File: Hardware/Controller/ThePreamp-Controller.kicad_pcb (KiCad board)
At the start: 2 copper layers, 60 x 95.8 mm, 34 parts, among them J1 B1 Relays, J10 I2C (FUTURE USE), J11 ROTARY ENC & SWITCH 1, J12 ROTARY ENC & SWITCH 2, J13 IR RECV, J14 12V, J15 8V, J2 PWR AMP L 12V TRIGGER, J3 PWR AMP L SWITCH, J4 PWR AMP R 12V TRIGGER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

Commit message: Controller pcb dimensions added
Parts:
- removed C1: 0.1uF, Capacitor_SMD:C_0805_2012Metric_Pad1.15x1.40mm_HandSolder
- removed D1, D2: CD4148W, Diode_SMD:D_0805_2012Metric
- removed J1: B1 Relays, Connector_JST:JST_XH_B7B-XH-A_1x07_P2.50mm_Vertical
- removed J10: I2C (FUTURE USE), Connector_JST:JST_XH_B4B-XH-A_1x04_P2.50mm_Vertical
- removed J11: ROTARY ENC & SWITCH 1, Connector_JST:JST_XH_B5B-XH-A_1x05_P2.50mm_Vertical
- removed J12: ROTARY ENC & SWITCH 2, Connector_JST:JST_XH_B5B-XH-A_1x05_P2.50mm_Vertical
- removed J13: IR RECV, Connector_JST:JST_XH_B3B-XH-A_1x03_P2.50mm_Vertical
- removed J2: PWR AMP L 12V TRIGGER, Connector_JST:JST_XH_B2B-XH-A_1x02_P2.50mm_Vertical
- removed J3: PWR AMP L SWITCH, Connector_JST:JST_XH_B2B-XH-A_1x02_P2.50mm_Vertical
- removed J4: PWR AMP R 12V TRIGGER, Connector_JST:JST_XH_B2B-XH-A_1x02_P2.50mm_Vertical
- removed J5: PWR AMP R SWITCH, Connector_JST:JST_XH_B2B-XH-A_1x02_P2.50mm_Vertical
- removed J6: PWR AMP TEMP NTC L, Connector_JST:JST_XH_B2B-XH-A_1x02_P2.50mm_Vertical
- removed J7: PWR AMP TEMP NTC R, Connector_JST:JST_XH_B2B-XH-A_1x02_P2.50mm_Vertical
- removed R1, R4: R, Resistor_THT:R_Axial_DIN0207_L6.3mm_D2.5mm_P10.16mm_Horizontal
- removed R7, R8: 10K, Resistor_SMD:R_0805_2012Metric_Pad1.15x1.40mm_HandSolder
- removed REF** (x4): MountingHole_3.2mm_M3_ISO7380, MountingHole:MountingHole_3.2mm_M3_ISO7380
- removed U2: AGQ20T03, AGQ20T03_footprint:AGQ20012
- removed U3: ULN2803ADWR, ULN2803:ULN2803ADWR
- removed U4: MCP23008-E_SO, MCP23008:MCP23008-E&slash_SO
- added  : , MountingHole:MountingHole_3.2mm_M3_ISO7380, F.Cu at (255.4, 101.0)
- added  : , MountingHole:MountingHole_3.2mm_M3_ISO7380, F.Cu at (41.4, 101.0)
- added  : , MountingHole:MountingHole_3.2mm_M3_ISO7380, F.Cu at (148.4, 101.0)
- added  : , MountingHole:MountingHole_3.2mm_M3_ISO7380, F.Cu at (148.4, 67.0)
- added  : , MountingHole:MountingHole_3.2mm_M3_ISO7380, F.Cu at (41.4, 67.0)
- added  : , MountingHole:MountingHole_3.2mm_M3_ISO7380, F.Cu at (255.4, 67.0)
- added SW1: RotaryEncoder_Switch, Rotary_Encoder:RotaryEncoder_Alps_EC11E-Switch_Vertical_H20mm, F.Cu at (25.8, 91.2)
- added SW2: RotaryEncoder_Switch, Rotary_Encoder:RotaryEncoder_Alps_EC11E-Switch_Vertical_H20mm, F.Cu at (265.9, 91.2)
- J14, J15, R10, R9, U5, U6: moved to B.Cu
- U1: value AGQ20T03 -> TSOP382xx; footprint AGQ20T03_footprint:AGQ20012 -> OptoDevice:Vishay_MINICAST-3Pin
- moved J15 131.9 mm to (41.1, 114.9), turned to 180 degrees
- moved J14 121.8 mm to (29.0, 114.8), turned to 180 degrees
- moved R9 86.8 mm to (213.8, 73.3), turned to 90 degrees
- moved U5 79.5 mm to (219.6, 79.9)
- moved R10 75.3 mm to (219.6, 84.5)
- moved U6 71.7 mm to (219.1, 89.9)
- moved J8 66.5 mm to (176.6, 152.0), turned to 0 degrees
- moved J9 39.0 mm to (155.2, 152.0), turned to 0 degrees
- moved U1 17.0 mm to (145.9, 88.7), turned to 0 degrees
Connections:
- J9 pad 5: CONTRAST(LCD) -> unconnected-(J9-Pin_5-Pad5)
- U1 pad 1: Net-(D1-Pad1) -> IR OUT
- U1 pad 2: unconnected-(U1-Pad2) -> GND
- U1 pad 3: Net-(J3-Pad1) -> +3V3
- U6 pad 19: NTC_R -> unconnected-(U6-D34-Pad19)
- U6 pad 20: NTC_L -> unconnected-(U6-D35-Pad20)
- U6 pad 22: CONTRAST(LCD) -> unconnected-(U6-D33-Pad22)
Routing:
- net +3V3: track 150.7 -> 27.8 mm
- net CONTRAST(LCD): track 98.9 -> 0.00 mm
- net +12V: track 67.7 -> 0.00 mm
- net NTC_L: track 65.6 -> 0.00 mm
- net +8V: track 63.9 -> 0.00 mm
- net I2C:SDA: track 78.6 -> 15.4 mm, vias 3 -> 1
- net I2C:SCL: track 76.1 -> 16.8 mm, vias 1 -> 0
- net SPI:MOSI: track 53.7 -> 9.94 mm
- net IR OUT: track 35.0 -> 0.00 mm
- net NTC_R: track 32.4 -> 0.00 mm
- net Net-(J1-Pad6): track 32.0 -> 0.00 mm
- net Net-(J1-Pad5): track 29.7 -> 0.00 mm
- net CW_1: track 27.8 -> 0.00 mm
- net Net-(J1-Pad4): track 27.4 -> 0.00 mm
- net Net-(J1-Pad2): track 26.7 -> 0.00 mm
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- removed copper zone on B.Cu, net GND
- removed copper zone on F.Cu, net GND
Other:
- board size 60 x 95.8 mm -> 270 x 61.6 mm
- board text added: "To-Do: check pins på IR-modtager, placering af IR-modtager (hul i front mellem displays vil være skjult bag acryl), pins på rotary encoders"

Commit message: Displays changed to SPI
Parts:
- removed J8: MUSES 72320 (SPI), Connector_JST:JST_XH_B6B-XH-A_1x06_P2.50mm_Vertical
- added J1: Digital Out, Connector_JST:JST_XH_B8B-XH-A_1x08_P2.50mm_Vertical, F.Cu at (51.0, 115.2)
- added J2: SPI DISPLAY 2, Connector_PinHeader_2.54mm:PinHeader_1x07_P2.54mm_Vertical, F.Cu at (163.0, 80.8)
- J9: value I2C DISPLAY (OLED/LCD) -> SPI DISPLAY 1; footprint Connector_JST:JST_XH_B5B-XH-A_1x05_P2.50mm_Vertical -> Connector_PinHeader_2.54mm:PinHeader_1x07_P2.54mm_Vertical
- U1: value TSOP382xx -> TSOP34838; footprint OptoDevice:Vishay_MINICAST-3Pin -> OptoDevice:Vishay_MOLD-3Pin
- moved J9 130.6 mm to (46.5, 79.5)
- moved R10 125.2 mm to (94.4, 83.0)
- moved U5 125.2 mm to (94.4, 78.4)
- moved U6 125.2 mm to (93.9, 88.5)
- moved R9 125.2 mm to (88.6, 71.8)
- moved U1 1.98 mm to (145.8, 90.6)
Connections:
- J9 pad 1: I2C:SCL -> GND
- J9 pad 2: I2C:SDA -> +3V3
- J9 pad 3: GND -> SPI:SCK
- J9 pad 4: +3V3 -> SPI:MOSI
- U6 pad 19: unconnected-(U6-D34-Pad19) -> SPI:SS_DISPLAY_1
- U6 pad 20: unconnected-(U6-D35-Pad20) -> SPI:SS_DISPLAY_2
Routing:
- net I2C:SCL: track 16.8 -> 0.00 mm
- net I2C:SDA: track 15.4 -> 4.13 mm, vias 1 -> 0
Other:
- board text added: "To-Do: placering af IR-modtager (hul i front mellem displays vil være skjult bag acryl), pins på rotary encoders, stik typer, SPI til displays"
- board text removed: "To-Do: check pins på IR-modtager, placering af IR-modtager (hul i front mellem displays vil være skjult bag acryl), pins på rotary encoders"

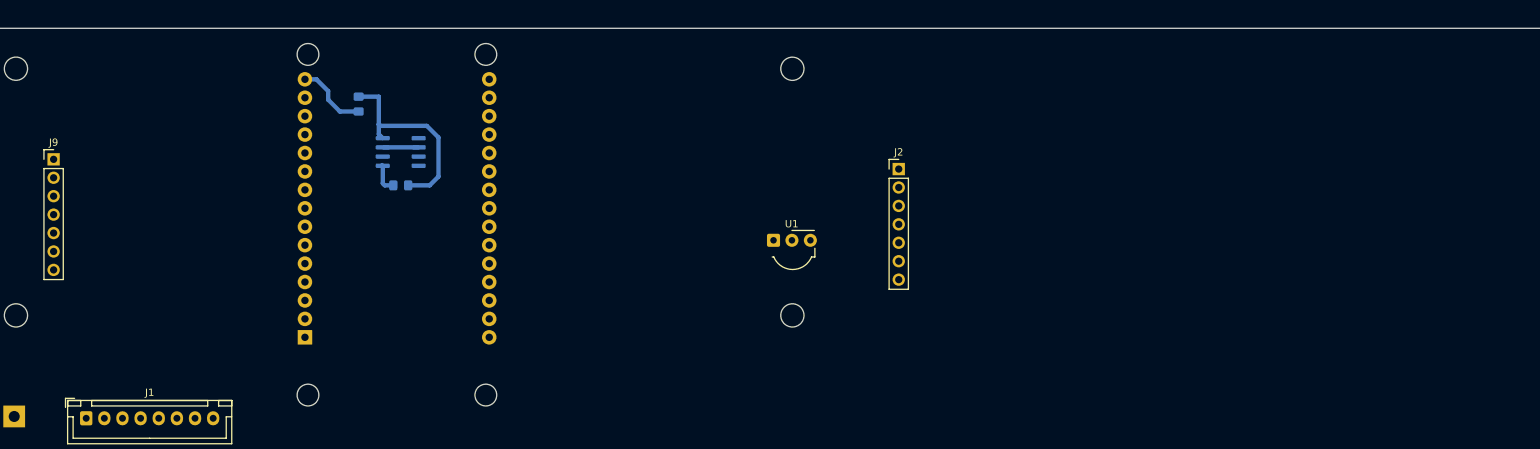
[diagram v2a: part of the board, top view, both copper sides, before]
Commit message: Pins updated
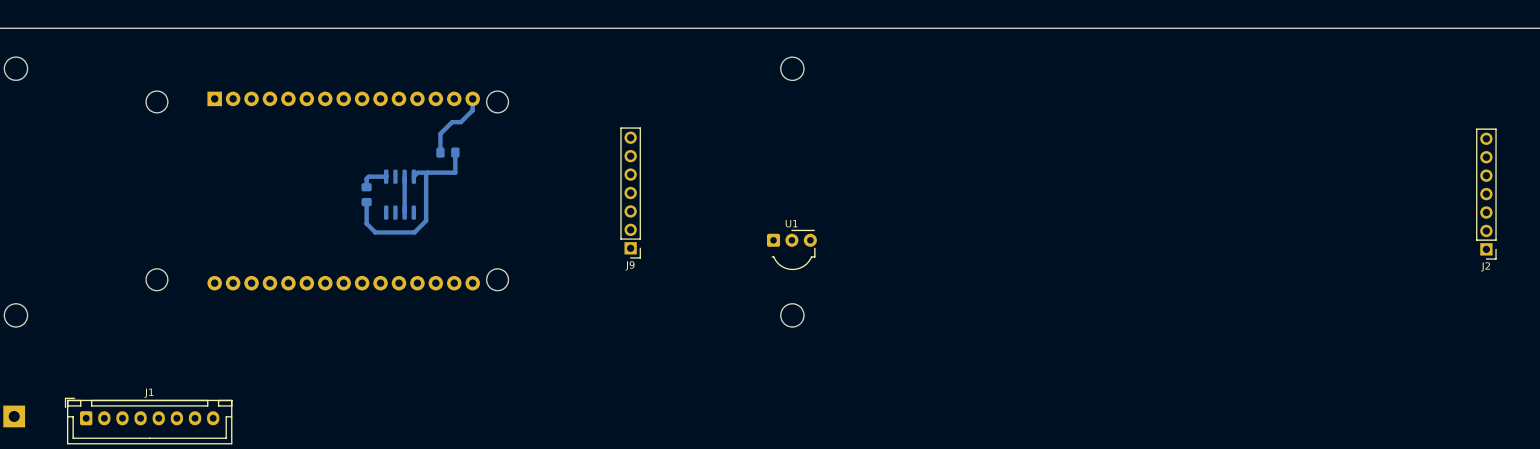
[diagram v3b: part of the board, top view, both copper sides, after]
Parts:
- moved J2 81.7 mm to (244.0, 91.9), turned to 180 degrees
- moved J9 80.5 mm to (126.1, 91.7), turned to 180 degrees
- moved R9 14.0 mm to (100.9, 78.5), turned to 0 degrees
- moved U6 10.7 mm to (84.3, 83.8), turned to -90 degrees
- moved U5 5.88 mm to (94.3, 84.3), turned to 90 degrees
- moved R10 4.87 mm to (89.7, 84.3), turned to -90 degrees
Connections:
- net SPI:SS renamed SPI:SS_MUSES
- J2 pad 5: unconnected-(J2-Pin_5-Pad5) -> SPI:RESET_DISPLAY_2
- J2 pad 6: unconnected-(J2-Pin_6-Pad6) -> SPI:DC
- J9 pad 5: unconnected-(J9-Pin_5-Pad5) -> SPI:RESET_DISPLAY_1
- J9 pad 6: unconnected-(J9-Pin_6-Pad6) -> SPI:DC
- U1 pad 1: IR OUT -> IR RECV
- U6 pad 19: SPI:SS_DISPLAY_1 -> SW_1
- U6 pad 20: SPI:SS_DISPLAY_2 -> SW_2
- U6 pad 21: IR OUT -> SPI:RESET_DISPLAY_1
- U6 pad 22: unconnected-(U6-D33-Pad22) -> SPI:RESET_DISPLAY_2
- U6 pad 25: SW_1 -> CW_2
- U6 pad 26: CW_2 -> CCW_2
- U6 pad 27: CCW_2 -> SPI:SS_DISPLAY_1
- U6 pad 28: SW_2 -> SPI:SS_DISPLAY_2
- U6 pad 3: unconnected-(U6-D15-Pad3) -> IR RECV
- U6 pad 5: unconnected-(U6-D4-Pad5) -> SPI:DC

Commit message: Add power relay control output
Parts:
- removed J14: 12V, TerminalBlock:TerminalBlock_bornier-2_P5.08mm
- removed J15: 8V, TerminalBlock:TerminalBlock_bornier-2_P5.08mm
- removed J9: SPI DISPLAY 1, Connector_PinHeader_2.54mm:PinHeader_1x07_P2.54mm_Vertical
- removed R10, R9: 4K7, Resistor_SMD:R_0805_2012Metric_Pad1.15x1.40mm_HandSolder
- removed U5: 24C02C_SN, Package_SO:SOIC-8-1EP_3.9x4.9mm_P1.27mm_EP2.41x3.3mm
- removed U6: ESP32-DEVKIT-V1, ESP32FP:MODULE_ESP32_DEVKIT_V1
- added J3: SPI DISPLAY 1, Connector_PinHeader_2.54mm:PinHeader_1x07_P2.54mm_Vertical, F.Cu at (124.5, 91.7)
- added J4: SPI DISPLAY 2, Connector_PinHeader_2.54mm:PinHeader_1x07_P2.54mm_Vertical, F.Cu at (242.1, 91.8)
- added J5: Power relay trigger, Connector_JST:JST_XH_B2B-XH-A_1x02_P2.50mm_Vertical, B.Cu at (32.9, 118.6)
- added R3: 330R, Resistor_SMD:R_0805_2012Metric_Pad1.20x1.40mm_HandSolder, B.Cu at (33.6, 98.3)
- added U2: ESP32-DEVKIT-V1, ESP32FP:MODULE_ESP32_DEVKIT_V1, B.Cu at (87.7, 83.7)
- added U3: TSOP34838, OptoDevice:Vishay_MOLD-3Pin, F.Cu at (145.8, 93.4)
- added U4: PC817, Package_DIP:DIP-4_W7.62mm, B.Cu at (32.3, 101.5)
- J1: value Digital Out -> 8V; footprint Connector_JST:JST_XH_B8B-XH-A_1x08_P2.50mm_Vertical -> TerminalBlock:TerminalBlock_bornier-2_P5.08mm; moved to B.Cu
- J2: value SPI DISPLAY 2 -> Digital Out; footprint Connector_PinHeader_2.54mm:PinHeader_1x07_P2.54mm_Vertical -> Connector_JST:JST_XH_B8B-XH-A_1x08_P2.50mm_Vertical; moved to B.Cu
- U1: value TSOP34838 -> 24C02C_SN; footprint OptoDevice:Vishay_MOLD-3Pin -> Package_SO:SOIC-8-1EP_3.9x4.9mm_P1.27mm_EP2.41x3.3mm; moved to B.Cu
- moved J2 202.8 mm to (43.0, 118.6), turned to 0 degrees
- moved U1 51.1 mm to (95.2, 83.3)
- moved J1 32.5 mm to (18.6, 117.3)
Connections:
- J1 pad 1: I2C:SDA -> +8V
- J1 pad 2: I2C:SCL -> GND
- J2 pad 1: GND -> I2C:SDA
- J2 pad 2: +3V3 -> I2C:SCL
- J2 pad 3: SPI:SCK -> GND
- J2 pad 4: SPI:MOSI -> +3V3
- J2 pad 5: SPI:RESET_DISPLAY_2 -> SPI:SCK
- J2 pad 6: SPI:DC -> SPI:MISO
- J2 pad 7: SPI:SS_DISPLAY_2 -> SPI:MOSI
- SW1 pad A: unconnected-(SW1-PadA) -> CCW_1
- SW1 pad B: unconnected-(SW1-PadB) -> CW_1
- SW1 pad C: unconnected-(SW1-PadC) -> GND
- SW2 pad A: unconnected-(SW2-PadA) -> CCW_2
- SW2 pad B: unconnected-(SW2-PadB) -> CW_2
- SW2 pad C: unconnected-(SW2-PadC) -> GND
- U1 pad 1: IR RECV -> GND
- U1 pad 3: +3V3 -> GND
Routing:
- net +3V3: track 27.8 -> 0.00 mm
- net SPI:MOSI: track 9.94 -> 0.00 mm
- net GND: track 4.95 -> 0.00 mm
- net I2C:SDA: track 4.13 -> 0.00 mm
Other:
- board text added: "The Preamp Controller by Grønning & Tofft (2024)"
- board text added: "To-Do: placering af IR-modtager (hul i front mellem displays vil være skjult bag acryl), stik typer, footprint til display, fastgørelse af display"
- board text removed: "0x20"
- board text removed: "Pre-amp controller by Carsten Grønning & Jan Tofft (2022)"
- board text removed: "To-Do: placering af IR-modtager (hul i front mellem displays vil være skjult bag acryl), pins på rotary encoders, stik typer, SPI til displays"

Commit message: Added symbol/footprint for display
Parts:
- J3, J4: footprint Connector_PinHeader_2.54mm:PinHeader_1x07_P2.54mm_Vertical -> OLED SPI 2.08:OLED SPI 2.08
- moved J3 1.60 mm to (124.9, 93.3)
- moved J4 1.49 mm to (241.9, 93.3)
- moved R3 1.39 mm to (34.2, 99.5)
- moved U4 1.27 mm to (32.9, 102.6)
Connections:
- U4 pad 3: Net-(J5-Pin_1) -> Net-(J5-Pin_2)
- U4 pad 4: Net-(J5-Pin_2) -> Net-(J5-Pin_1)
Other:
- board text added: "To-Do: placering af IR-modtager (hul i front mellem displays vil være skjult bag acryl, men måske bedre ved siden af display), stik typer, ekstra stik til display, fastgørelse af display"
- board text removed: "To-Do: placering af IR-modtager (hul i front mellem displays vil være skjult bag acryl), stik typer, footprint til display, fastgørelse af display"

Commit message: Controller pcb is ready (except for connectors)
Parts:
- added C1: 100nF, Capacitor_SMD:C_0805_2012Metric_Pad1.18x1.45mm_HandSolder, B.Cu at (101.4, 84.9)
- added C2: 100nF, Capacitor_SMD:C_0805_2012Metric_Pad1.18x1.45mm_HandSolder, F.Cu at (115.7, 90.3)
- added C3: 100nF, Capacitor_SMD:C_0805_2012Metric_Pad1.18x1.45mm_HandSolder, F.Cu at (232.8, 90.3)
- added C4: 22uF, Capacitor_SMD:C_1206_3216Metric_Pad1.33x1.80mm_HandSolder, F.Cu at (113.5, 90.9)
- added C5: 22uF, Capacitor_SMD:C_1206_3216Metric_Pad1.33x1.80mm_HandSolder, F.Cu at (230.0, 90.9)
- added C6: 470uF, EEE_FH1C471L:CAP_EEEFH1C471L, B.Cu at (21.9, 105.8)
- R3: moved to F.Cu
- U1: value 24C02C_SN -> CAT24C64WI-GT3; footprint Package_SO:SOIC-8-1EP_3.9x4.9mm_P1.27mm_EP2.41x3.3mm -> footprints:SOIC8_ONS
- U4: value PC817 -> APC-817B1-SL; footprint Package_DIP:DIP-4_W7.62mm -> APC_817B1_SL:APC-817xx-SL_AMB-M; moved to F.Cu
- moved U4 3.66 mm to (34.1, 106.0)
- moved R3 2.15 mm to (34.2, 97.4)
- moved J1 0.90 mm to (19.5, 117.5)
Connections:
- U4 pad 3: Net-(J5-Pin_2) -> Net-(J5-Pin_1)
- U4 pad 4: Net-(J5-Pin_1) -> Net-(J5-Pin_2)
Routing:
- net SPI:DC: track 0.00 -> 270.7 mm
- net SPI:MOSI: track 0.00 -> 230.5 mm
- net +3V3: track 0.00 -> 222.0 mm
- net SW_2: track 0.00 -> 197.2 mm
- net SPI:SCK: track 0.00 -> 196.9 mm
- net CW_2: track 0.00 -> 190.0 mm
- net CCW_2: track 0.00 -> 181.4 mm
- net SPI:RESET_DISPLAY_2: track 0.00 -> 157.9 mm, vias 0 -> 1
- net GND: track 0.00 -> 147.2 mm, vias 0 -> 7
- net SPI:SS_DISPLAY_2: track 0.00 -> 141.8 mm, vias 0 -> 1
- net +8V: track 0.00 -> 134.8 mm
- net I2C:SCL: track 0.00 -> 85.0 mm
- net CCW_1: track 0.00 -> 74.0 mm
- net I2C:SDA: track 0.00 -> 71.3 mm
- net CW_1: track 0.00 -> 63.0 mm
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- added copper zone on B.Cu, net GND
- added copper zone on F.Cu, net GND

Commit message: Moved digital connector to match analog pcb
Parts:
- moved J2 189.8 mm to (232.8, 117.7), turned to 180 degrees
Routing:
- net I2C:SCL: track 85.0 -> 211.9 mm
- net I2C:SDA: track 71.3 -> 194.0 mm, vias 0 -> 1
- net SPI:MISO: track 34.1 -> 151.3 mm, vias 1 -> 0
- net SPI:SS_MUSES: track 34.2 -> 139.7 mm
- net +3V3: track 222.0 -> 290.0 mm
- net SPI:MOSI: track 230.5 -> 215.8 mm
- net GND: track 147.2 -> 150.8 mm, vias 7 -> 11
- net SPI:SCK: track 196.9 -> 194.9 mm
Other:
- board text added: "To-Do: stik typer, ekstra stik til display, fastgørelse af display"
- board text removed: "To-Do: placering af IR-modtager (hul i front mellem displays vil være skjult bag acryl, men måske bedre ved siden af display), stik typer, ekstra stik til display, fastgørelse af display"

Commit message: Digital connector (IDC 16) aligned on controller and analog board
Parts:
- removed C6: 470uF, EEE_FH1C471L:CAP_EEEFH1C471L
- J2: footprint Connector_JST:JST_XH_B8B-XH-A_1x08_P2.50mm_Vertical -> Connector_IDC:IDC-Header_2x08_P2.54mm_Vertical
- U1: footprint footprints:SOIC8_ONS -> footprints:SOIC8_ONS-M
- moved SW1 247.5 mm to (270.9, 57.0), turned to -90 degrees
- moved SW2 237.4 mm to (30.9, 57.1), turned to -90 degrees
- moved   220.7 mm to (255.4, 47.3), turned to 180 degrees
- moved   220.6 mm to (41.4, 47.3), turned to 180 degrees
- moved   214.5 mm to (255.4, 81.3), turned to 180 degrees
- moved   214.5 mm to (41.4, 81.3), turned to 180 degrees
- moved J4 190.8 mm to (54.9, 55.0), turned to 0 degrees
- moved C3 171.8 mm to (64.0, 58.0), turned to 90 degrees
- moved C5 166.6 mm to (66.8, 57.4), turned to 90 degrees
- moved U2 122.8 mm to (209.0, 64.5), turned to -90 degrees
- moved U1 107.9 mm to (201.5, 65.0), turned to 180 degrees
- moved C1 96.4 mm to (195.3, 63.4), turned to -90 degrees
- moved C4 77.4 mm to (183.3, 57.4), turned to 90 degrees
- moved C2 72.9 mm to (181.0, 58.0), turned to 90 degrees
- moved J2 70.0 mm to (292.1, 80.5), turned to -90 degrees
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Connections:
- J2 pad 1: I2C:SDA -> SPI:SS_MUSES
- J2 pad 2: I2C:SCL -> GND
- J2 pad 3: GND -> SPI:MOSI
- J2 pad 4: +3V3 -> GND
- J2 pad 5: SPI:SCK -> SPI:MISO
- J2 pad 6: SPI:MISO -> GND
- J2 pad 7: SPI:MOSI -> SPI:SCK
- J2 pad 8: SPI:SS_MUSES -> +3V3
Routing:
- net Net-(U2-D2): track 61.6 -> 195.4 mm, vias 0 -> 1
- net GND: track 150.8 -> 31.4 mm, vias 11 -> 6
- net SPI:DC: track 270.7 -> 153.4 mm, vias 0 -> 1
- net I2C:SCL: track 211.9 -> 140.2 mm
- net SPI:SCK: track 194.9 -> 257.1 mm
- net I2C:SDA: track 194.0 -> 133.5 mm
- net SPI:MISO: track 151.3 -> 99.9 mm
- net SPI:MOSI: track 215.8 -> 252.4 mm
- net +8V: track 134.8 -> 164.3 mm
- net SPI:SS_MUSES: track 139.7 -> 111.6 mm
- net +3V3: track 290.0 -> 314.7 mm
- net IR RECV: track 50.3 -> 52.9 mm
- net SW_1: track 48.8 -> 46.8 mm
- net CCW_1: track 74.0 -> 73.2 mm
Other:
- board size 270 x 61.6 mm -> 302.4 x 44.5 mm
- board text added: "3.3"
- board text added: "GND"
- board text added: "MISO"
- board text added: "MOSI"
- board text added: "SCK"
- board text added: "SCL"
- board text added: "SDA"
- board text added: "SS"
- board text added: "To-Do: stik typer, lyt på 8V"
- board text removed: "To-Do: stik typer, ekstra stik til display, fastgørelse af display"
